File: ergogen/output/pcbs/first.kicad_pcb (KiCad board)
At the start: 2 copper layers, 135 x 97 mm, 30 parts

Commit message: avance du pcb
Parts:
- added REF**: ADG732, ADG732, F.Cu at (101.5, 93.0)
- added REF**: RP2040 Zero, RP2040_Zero, F.Cu at (101.5, 133.0)

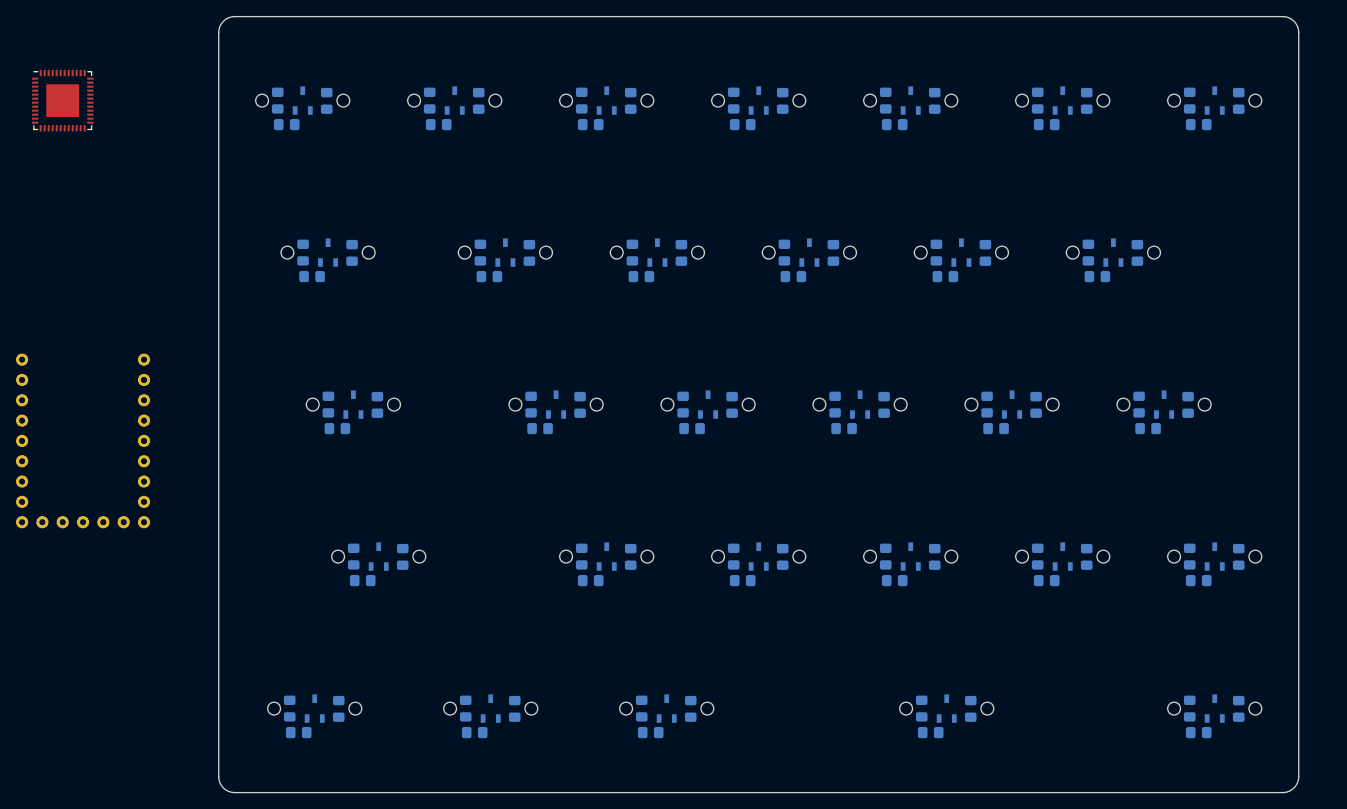
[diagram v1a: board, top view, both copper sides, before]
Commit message: avancement du pcb sur ergogen
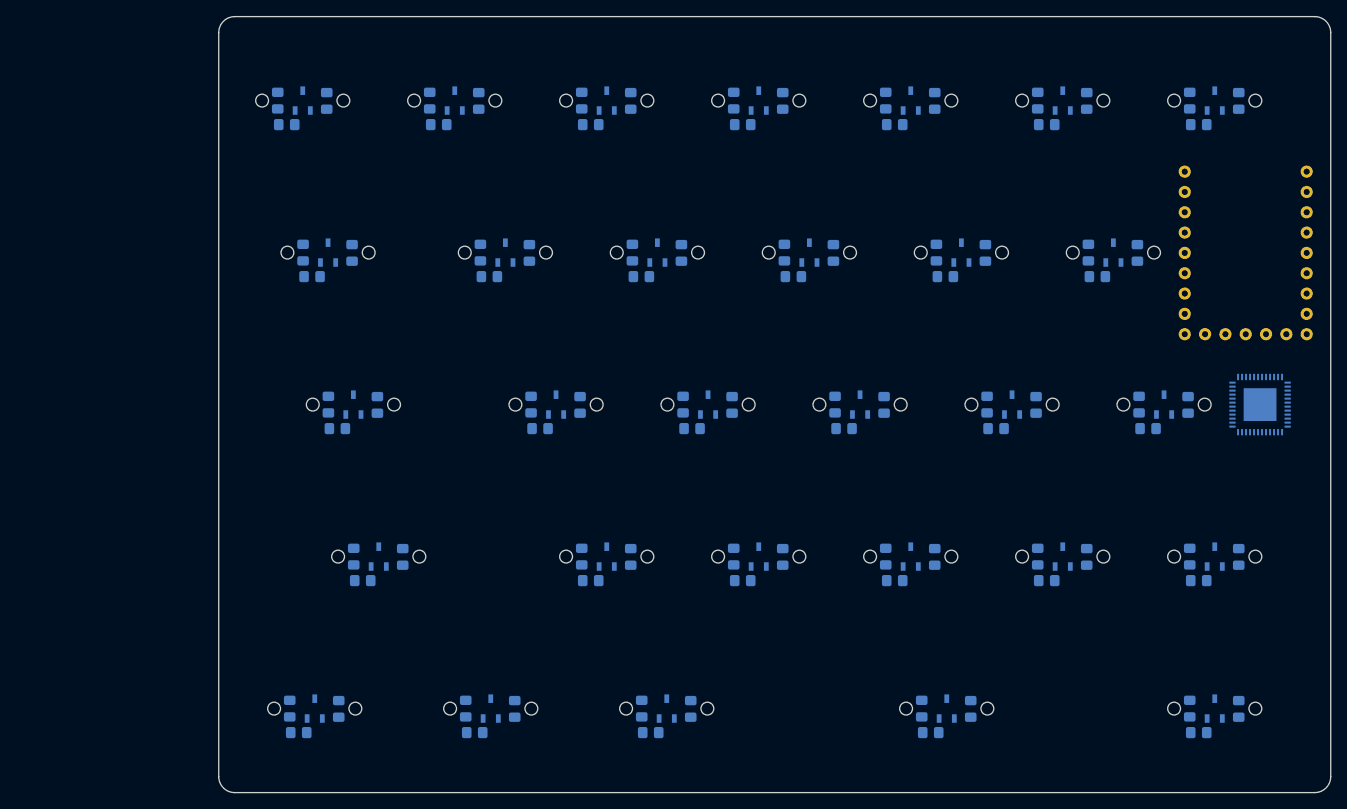
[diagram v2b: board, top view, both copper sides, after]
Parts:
- REF**: moved to B.Cu
- moved REF** 154.4 mm to (251.2, 131.0)
- moved REF** 147.2 mm to (246.8, 109.5)
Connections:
- REF** pad 1: (no net) -> col4_r2
- REF** pad 10: (no net) -> col2_r1
- REF** pad 11: key_col1_r1 -> col1_r1
- REF** pad 12: key_col0_r1 -> col0_r1
- REF** pad 2: (no net) -> col3_r2
- REF** pad 25: (no net) -> col3_r3
- REF** pad 26: (no net) -> col4_r3
- REF** pad 27: (no net) -> col5_r3
- REF** pad 28: (no net) -> col0_r4
- REF** pad 29: (no net) -> col1_r4
- REF** pad 3: (no net) -> col2_r2
- REF** pad 30: (no net) -> col2_r4
- REF** pad 31: (no net) -> col3_r4
- REF** pad 32: (no net) -> col4_r4
- REF** pad 33: (no net) -> col5_r4
- REF** pad 34: (no net) -> thumb0_r5
- REF** pad 35: (no net) -> thumb1_r5
- REF** pad 36: (no net) -> thumb2_r5
- REF** pad 37: (no net) -> thumb3_r5
- REF** pad 38: (no net) -> thumb4_r5
- REF** pad 4: (no net) -> col1_r2
- REF** pad 45: (no net) -> col2_r3
- REF** pad 46: (no net) -> col1_r3
- REF** pad 47: (no net) -> col0_r3
- REF** pad 48: (no net) -> col5_r2
- REF** pad 5: (no net) -> col0_r2
- REF** pad 6: (no net) -> col6_r1
- REF** pad 7: (no net) -> col5_r1
- REF** pad 8: (no net) -> col4_r1
- REF** pad 9: (no net) -> col3_r1
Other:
- board size 135 x 97 mm -> 139 x 97 mm

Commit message: début kicad
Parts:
- moved REF** 8.00 mm to (254.8, 109.5), turned to -90 degrees
- moved REF** 2.00 mm to (253.2, 131.0)
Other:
- board size 139 x 97 mm -> 143.5 x 97 mm
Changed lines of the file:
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@@
     (footprint "ADG732"
       (layer "B.Cu")
-      (at 251.1666667 131 0)
+      (at 253.1666667 131 0)
       (property "Reference" "REF**"
         (at 0 -4.8 0)
@@
     (footprint "RP2040_Zero"
       (layer "F.Cu")
-      (at 246.83333340000001 109.5 0)
+      (at 254.83333340000001 109.5 -90)
       (property "Reference" "REF**"
         (at 1.27 0 0)
@@
     )
   (gr_line (start 121 177.5) (end 121 84.5) (angle 90) (layer Edge.Cuts) (width 0.15))
-(gr_line (start 123 82.5) (end 258.0000001 82.5) (angle 90) (layer Edge.Cuts) (width 0.15))
-(gr_line (start 260.0000001 84.5) (end 260.0000001 177.5) (angle 90) (layer Edge.Cuts) (width 0.15))
-(gr_line (start 258.0000001 179.5) (end 123 179.5) (angle 90) (layer Edge.Cuts) (width 0.15))
+(gr_line (start 123 82.5) (end 262.5000001 82.5) (angle 90) (layer Edge.Cuts) (width 0.15))
+(gr_line (start 264.5000001 84.5) (end 264.5000001 177.5) (angle 90) (layer Edge.Cuts) (width 0.15))
+(gr_line (start 262.5000001 179.5) (end 123 179.5) (angle 90) (layer Edge.Cuts) (width 0.15))
 (gr_arc (start 123 84.5) (end 123 82.5) (angle -90) (layer Edge.Cuts) (width 0.15))
-(gr_arc (start 258.0000001 84.5) (end 260.0000001 84.5) (angle -90) (layer Edge.Cuts) (width 0.15))
-(gr_arc (start 258.0000001 177.5) (end 258.0000001 179.5) (angle -90) (layer Edge.Cuts) (width 0.15))
+(gr_arc (start 262.5000001 84.5) (end 264.5000001 84.5) (angle -90) (layer Edge.Cuts) (width 0.15))
+(gr_arc (start 262.5000001 177.5) (end 262.5000001 179.5) (angle -90) (layer Edge.Cuts) (width 0.15))
 (gr_arc (start 123 177.5) (end 121 177.5) (angle -90) (layer Edge.Cuts) (width 0.15))
 )

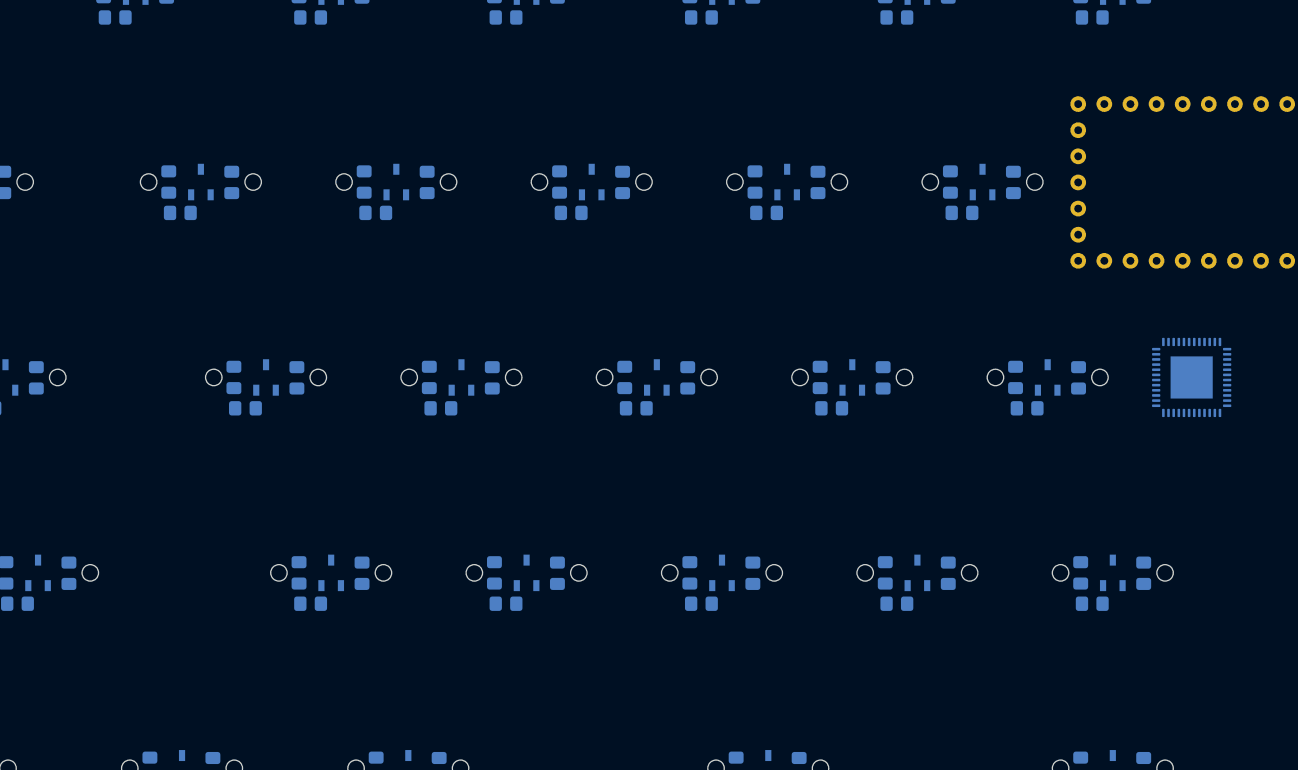
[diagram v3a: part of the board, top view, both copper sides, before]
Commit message: ajout des trous de vis
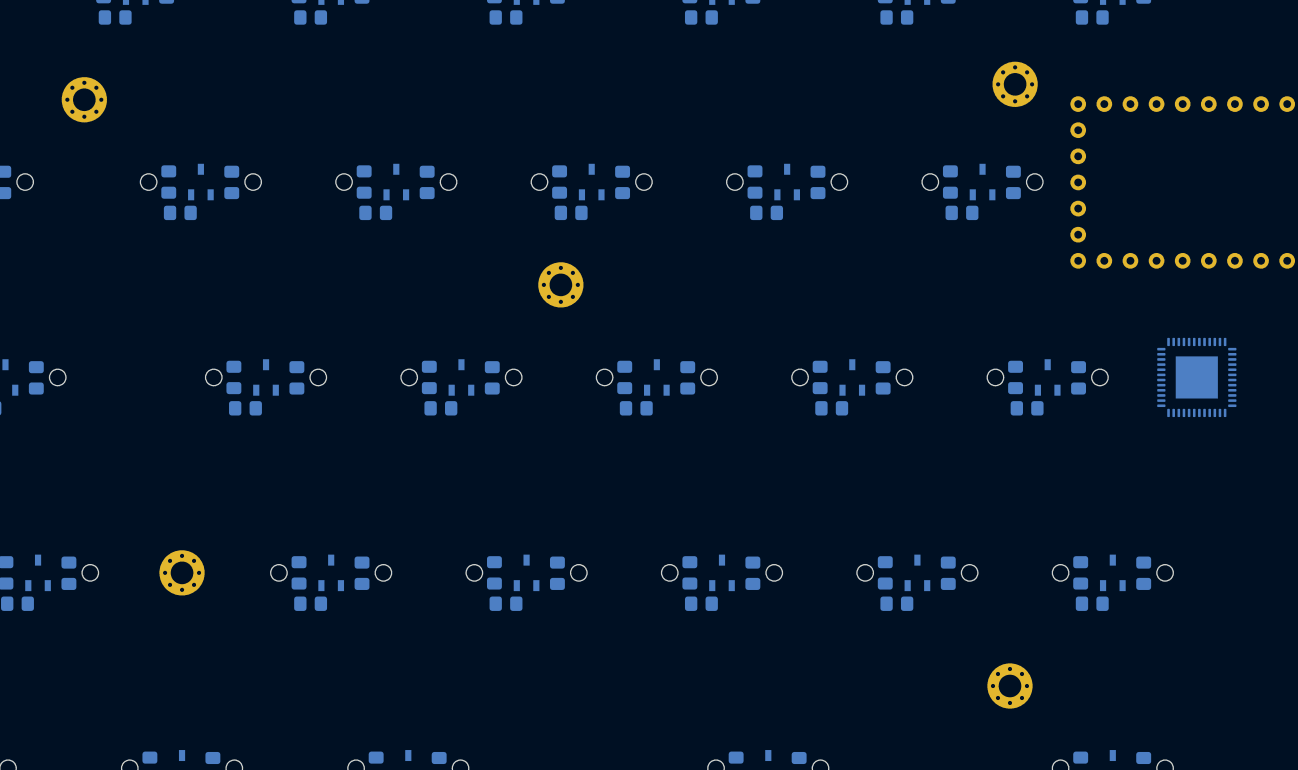
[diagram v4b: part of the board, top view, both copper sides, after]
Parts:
- added _1: , MountingHole_2.2mm_M2_Pad_Via, F.Cu at (145.5, 104.0)
- added _2: , MountingHole_2.2mm_M2_Pad_Via, F.Cu at (236.0, 102.5)
- added _3: , MountingHole_2.2mm_M2_Pad_Via, F.Cu at (235.5, 161.0)
- added _4: , MountingHole_2.2mm_M2_Pad_Via, F.Cu at (155.0, 150.0)
- added _5: , MountingHole_2.2mm_M2_Pad_Via, F.Cu at (191.8, 122.0)
- moved REF** 0.50 mm to (253.7, 131.0)
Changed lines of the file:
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@@
       (pad "3" smd rect (at 0 -1.24 270) (size 1.07 0.6) (layers "B.Cu" "B.Mask" "B.Paste") (net 2 "GND"))
+    )
+    (module "MountingHole_2.2mm_M2_Pad_Via" (version 20210722) (generator pcbnew) (layer "F.Cu")
+      (at 145.49999989999998 104 0)
+      (fp_text reference "_1" (at 0 -3.2) (layer "F.SilkS") hide
+        (effects (font (size 1 1) (thickness 0.15)))
+      )
+      (fp_circle (center 0 0) (end 2.45 0) (layer "F.CrtYd") (width 0.05) (fill none))
+      (pad "1" thru_hole circle locked (at 1.166726 1.166726) (size 0.7 0.7) (drill 0.4) (layers *.Cu *.Mask))
+      (pad "1" thru_hole circle locked (at 0 0) (size 4.4 4.4) (drill 2.2) (layers *.Cu *.Mask))
+      (pad "1" thru_hole circle locked (at 0 1.65) (size 0.7 0.7) (drill 0.4) (layers *.Cu *.Mask))
+      (pad "1" thru_hole circle locked (at 1.166726 -1.166726) (size 0.7 0.7) (drill 0.4) (layers *.Cu *.Mask))
+      (pad "1" thru_hole circle locked (at -1.65 0) (size 0.7 0.7) (drill 0.4) (layers *.Cu *.Mask))
+      (pad "1" thru_hole circle locked (at -1.166726 -1.166726) (size 0.7 0.7) (drill 0.4) (layers *.Cu *.Mask))
+      (pad "1" thru_hole circle locked (at -1.166726 1.166726) (size 0.7 0.7) (drill 0.4) (layers *.Cu *.Mask))
+      (pad "1" thru_hole circle locked (at 1.65 0) (size 0.7 0.7) (drill 0.4) (layers *.Cu *.Mask))
+      (pad "1" thru_hole circle locked (at 0 -1.65) (size 0.7 0.7) (drill 0.4) (layers *.Cu *.Mask))
+    )
+    (module "MountingHole_2.2mm_M2_Pad_Via" (version 20210722) (generator pcbnew) (layer "F.Cu")
+      (at 236.00000010000002 102.5 0)
+      (fp_text reference "_2" (at 0 -3.2) (layer "F.SilkS") hide
+        (effects (font (size 1 1) (thickness 0.15)))
+      )
+      (fp_circle (center 0 0) (end 2.45 0) (layer "F.CrtYd") (width 0.05) (fill none))
+      (pad "1" thru_hole circle locked (at 1.166726 1.166726) (size 0.7 0.7) (drill 0.4) (layers *.Cu *.Mask))
+      (pad "1" thru_hole circle locked (at 0 0) (size 4.4 4.4) (drill 2.2) (layers *.Cu *.Mask))
+      (pad "1" thru_hole circle locked (at 0 1.65) (size 0.7 0.7) (drill 0.4) (layers *.Cu *.Mask))
+      (pad "1" thru_hole circle locked (at 1.166726 -1.166726) (size 0.7 0.7) (drill 0.4) (layers *.Cu *.Mask))
+      (pad "1" thru_hole circle locked (at -1.65 0) (size 0.7 0.7) (drill 0.4) (layers *.Cu *.Mask))
+      (pad "1" thru_hole circle locked (at -1.166726 -1.166726) (size 0.7 0.7) (drill 0.4) (layers *.Cu *.Mask))
+      (pad "1" thru_hole circle locked (at -1.166726 1.166726) (size 0.7 0.7) (drill 0.4) (layers *.Cu *.Mask))
+      (pad "1" thru_hole circle locked (at 1.65 0) (size 0.7 0.7) (drill 0.4) (layers *.Cu *.Mask))
+      (pad "1" thru_hole circle locked (at 0 -1.65) (size 0.7 0.7) (drill 0.4) (layers *.Cu *.Mask))
+    )
+    (module "MountingHole_2.2mm_M2_Pad_Via" (version 20210722) (generator pcbnew) (layer "F.Cu")
+      (at 235.5 161 0)
+      (fp_text reference "_3" (at 0 -3.2) (layer "F.SilkS") hide
+        (effects (font (size 1 1) (thickness 0.15)))
+      )
+      (fp_circle (center 0 0) (end 2.45 0) (layer "F.CrtYd") (width 0.05) (fill none))
+      (pad "1" thru_hole circle locked (at 1.166726 1.166726) (size 0.7 0.7) (drill 0.4) (layers *.Cu *.Mask))
+      (pad "1" thru_hole circle locked (at 0 0) (size 4.4 4.4) (drill 2.2) (layers *.Cu *.Mask))
+      (pad "1" thru_hole circle locked (at 0 1.65) (size 0.7 0.7) (drill 0.4) (layers *.Cu *.Mask))
+      (pad "1" thru_hole circle locked (at 1.166726 -1.166726) (size 0.7 0.7) (drill 0.4) (layers *.Cu *.Mask))
+      (pad "1" thru_hole circle locked (at -1.65 0) (size 0.7 0.7) (drill 0.4) (layers *.Cu *.Mask))
+      (pad "1" thru_hole circle locked (at -1.166726 -1.166726) (size 0.7 0.7) (drill 0.4) (layers *.Cu *.Mask))
+      (pad "1" thru_hole circle locked (at -1.166726 1.166726) (size 0.7 0.7) (drill 0.4) (layers *.Cu *.Mask))
+      (pad "1" thru_hole circle locked (at 1.65 0) (size 0.7 0.7) (drill 0.4) (layers *.Cu *.Mask))
+      (pad "1" thru_hole circle locked (at 0 -1.65) (size 0.7 0.7) (drill 0.4) (layers *.Cu *.Mask))
+    )
+    (module "MountingHole_2.2mm_M2_Pad_Via" (version 20210722) (generator pcbnew) (layer "F.Cu")
+      (at 155 150 0)
+      (fp_text reference "_4" (at 0 -3.2) (layer "F.SilkS") hide
+        (effects (font (size 1 1) (thickness 0.15)))
+      )
+      (fp_circle (center 0 0) (end 2.45 0) (layer "F.CrtYd") (width 0.05) (fill none))
+      (pad "1" thru_hole circle locked (at 1.166726 1.166726) (size 0.7 0.7) (drill 0.4) (layers *.Cu *.Mask))
+      (pad "1" thru_hole circle locked (at 0 0) (size 4.4 4.4) (drill 2.2) (layers *.Cu *.Mask))
+      (pad "1" thru_hole circle locked (at 0 1.65) (size 0.7 0.7) (drill 0.4) (layers *.Cu *.Mask))
+      (pad "1" thru_hole circle locked (at 1.166726 -1.166726) (size 0.7 0.7) (drill 0.4) (layers *.Cu *.Mask))
+      (pad "1" thru_hole circle locked (at -1.65 0) (size 0.7 0.7) (drill 0.4) (layers *.Cu *.Mask))
+      (pad "1" thru_hole circle locked (at -1.166726 -1.166726) (size 0.7 0.7) (drill 0.4) (layers *.Cu *.Mask))
+      (pad "1" thru_hole circle locked (at -1.166726 1.166726) (size 0.7 0.7) (drill 0.4) (layers *.Cu *.Mask))
+      (pad "1" thru_hole circle locked (at 1.65 0) (size 0.7 0.7) (drill 0.4) (layers *.Cu *.Mask))
+      (pad "1" thru_hole circle locked (at 0 -1.65) (size 0.7 0.7) (drill 0.4) (layers *.Cu *.Mask))
+    )
+    (module "MountingHole_2.2mm_M2_Pad_Via" (version 20210722) (generator pcbnew) (layer "F.Cu")
+      (at 191.83333340000001 122 0)
+      (fp_text reference "_5" (at 0 -3.2) (layer "F.SilkS") hide
+        (effects (font (size 1 1) (thickness 0.15)))
+      )
+      (fp_circle (center 0 0) (end 2.45 0) (layer "F.CrtYd") (width 0.05) (fill none))
+      (pad "1" thru_hole circle locked (at 1.166726 1.166726) (size 0.7 0.7) (drill 0.4) (layers *.Cu *.Mask))
+      (pad "1" thru_hole circle locked (at 0 0) (size 4.4 4.4) (drill 2.2) (layers *.Cu *.Mask))
+      (pad "1" thru_hole circle locked (at 0 1.65) (size 0.7 0.7) (drill 0.4) (layers *.Cu *.Mask))
+      (pad "1" thru_hole circle locked (at 1.166726 -1.166726) (size 0.7 0.7) (drill 0.4) (layers *.Cu *.Mask))
+      (pad "1" thru_hole circle locked (at -1.65 0) (size 0.7 0.7) (drill 0.4) (layers *.Cu *.Mask))
+      (pad "1" thru_hole circle locked (at -1.166726 -1.166726) (size 0.7 0.7) (drill 0.4) (layers *.Cu *.Mask))
+      (pad "1" thru_hole circle locked (at -1.166726 1.166726) (size 0.7 0.7) (drill 0.4) (layers *.Cu *.Mask))
+      (pad "1" thru_hole circle locked (at 1.65 0) (size 0.7 0.7) (drill 0.4) (layers *.Cu *.Mask))
+      (pad "1" thru_hole circle locked (at 0 -1.65) (size 0.7 0.7) (drill 0.4) (layers *.Cu *.Mask))
     )
     (footprint "ADG732"
       (layer "B.Cu")
-      (at 253.1666667 131 0)
+      (at 253.6666667 131 0)
       (property "Reference" "REF**"
         (at 0 -4.8 0)

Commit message: ajustement de la footprint
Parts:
- moved _2 0.50 mm to (236.0, 102.0)
- turned REF** to 180 degrees
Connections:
- REF** pad 1: (no net) -> GND (x30)
- REF** pad 2: col0_r4 -> VCC
- REF** pad 2: col2_r3 -> VCC
- REF** pad 2: col2_r2 -> VCC
- REF** pad 2: col2_r1 -> VCC
- REF** pad 2: col3_r4 -> VCC
- REF** pad 2: col3_r3 -> VCC
- REF** pad 2: col3_r2 -> VCC
- REF** pad 2: col3_r1 -> VCC
- REF** pad 2: col4_r4 -> VCC
- REF** pad 2: col4_r3 -> VCC
- REF** pad 2: col4_r2 -> VCC
- REF** pad 2: col0_r3 -> VCC
- REF** pad 2: col4_r1 -> VCC
- REF** pad 2: col5_r4 -> VCC
- REF** pad 2: col5_r3 -> VCC
- REF** pad 2: col5_r2 -> VCC
- REF** pad 2: col5_r1 -> VCC
- REF** pad 2: col6_r1 -> VCC
- REF** pad 2: col0_r5 -> VCC
- REF** pad 2: col1_r5 -> VCC
- REF** pad 2: col2_r5 -> VCC
- REF** pad 2: col3_r5 -> VCC
- REF** pad 2: col0_r2 -> VCC
- REF** pad 2: col4_r5 -> VCC
- REF** pad 2: col0_r1 -> VCC
- REF** pad 2: col1_r4 -> VCC
- REF** pad 2: col1_r3 -> VCC
- REF** pad 2: col1_r2 -> VCC
- REF** pad 2: col1_r1 -> VCC
- REF** pad 2: col2_r4 -> VCC

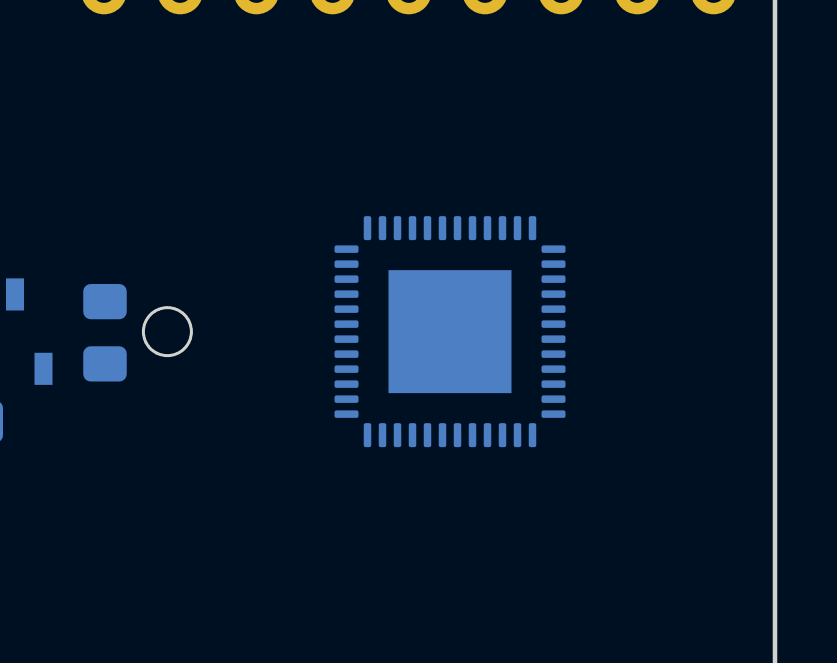
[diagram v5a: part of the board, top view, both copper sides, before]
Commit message: ADG732 ergogen
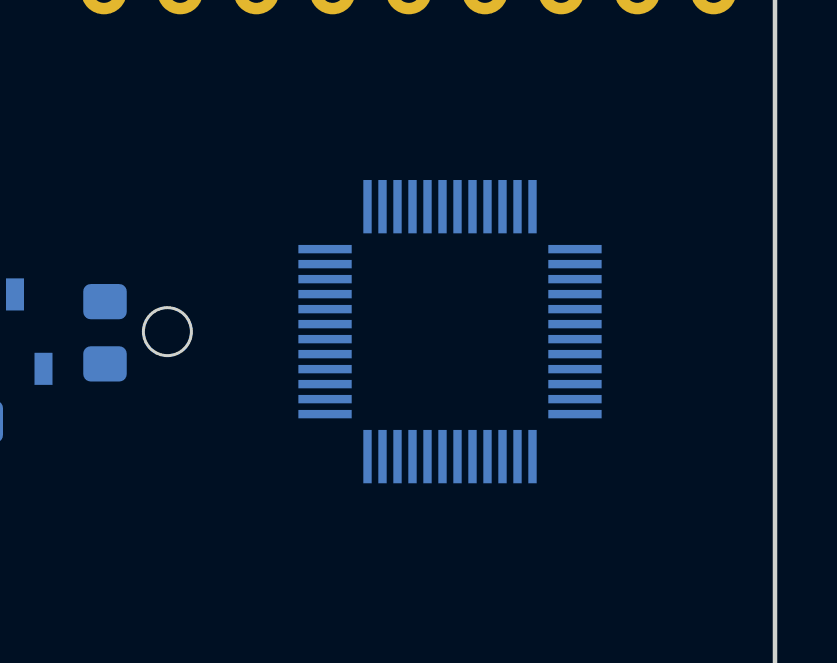
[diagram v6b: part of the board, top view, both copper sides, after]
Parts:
- removed the REF** at (253.7, 131.0)
- added REF**: ADG732BSUZ, ADG732_TQFP, B.Cu at (253.7, 131.0)
